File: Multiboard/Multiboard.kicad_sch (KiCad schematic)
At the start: 52 parts, among them J1 Conn_01x20_Socket, J2 Conn_01x20_Socket, J3 Debug, J4 USB_C_Receptacle_USB2.0_16P, SW1 BOOT0, SW2 NRST, SW8 KEY, U1 STM32F411RET6, U2 MAX662AESA_T, U3 MCP1792x-3302xCB, Y1 32.768KHz, Y2 25MHz

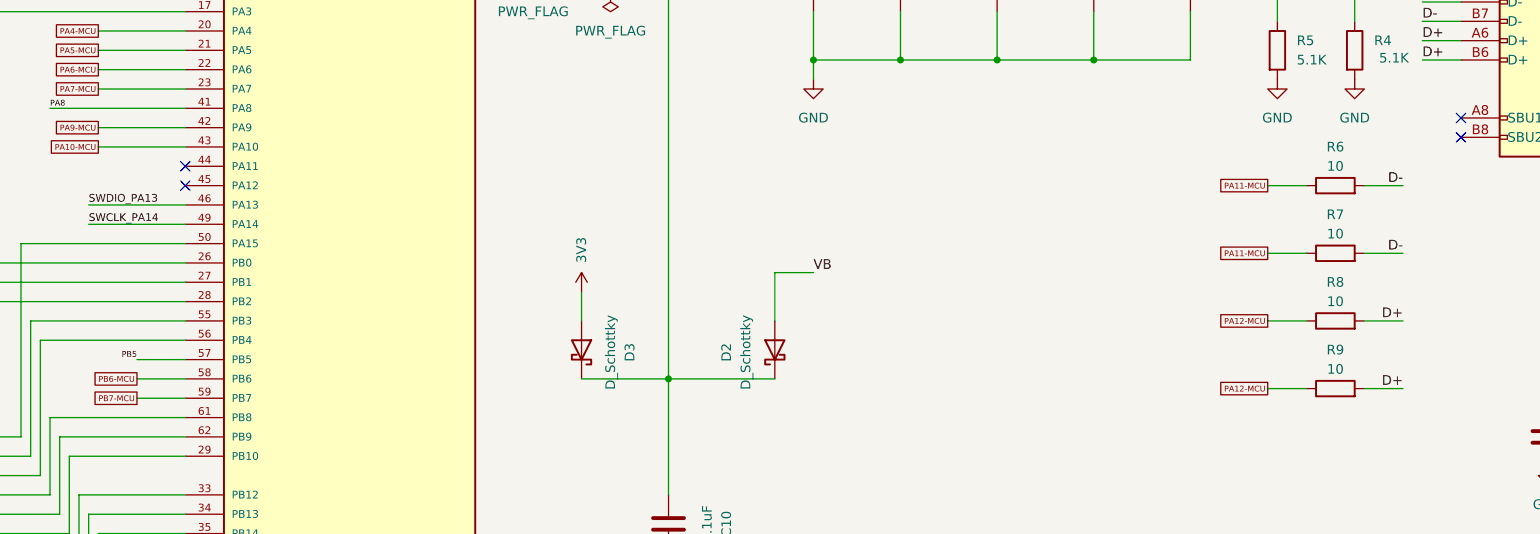
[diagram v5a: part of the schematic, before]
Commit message: positioned and wired ldo charge pump buttons leds and rtc circuit
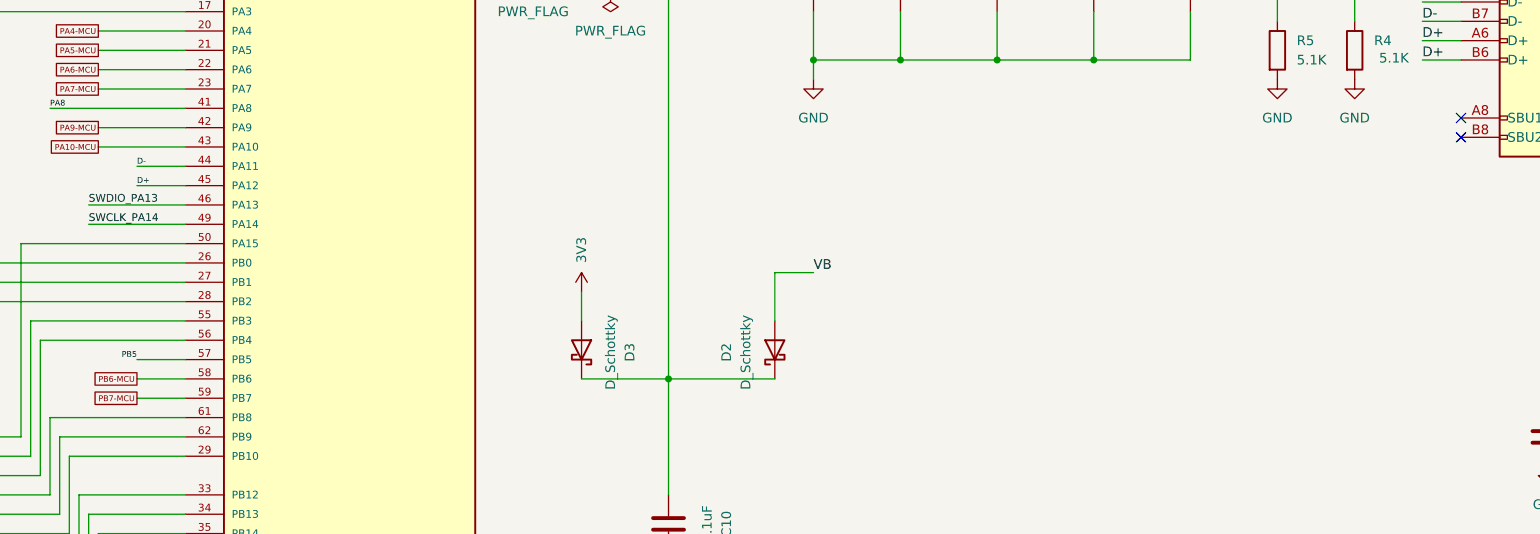
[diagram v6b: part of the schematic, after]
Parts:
- removed R6, R7, R8, R9: 10, Resistor_SMD:R_0603_1608Metric_Pad0.98x0.95mm_HandSolder, symbol Device:R
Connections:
- net D+: now also U1.45 (PA12)
- net D-: now also U1.44 (PA11)
- no-connect marks 14 -> 12

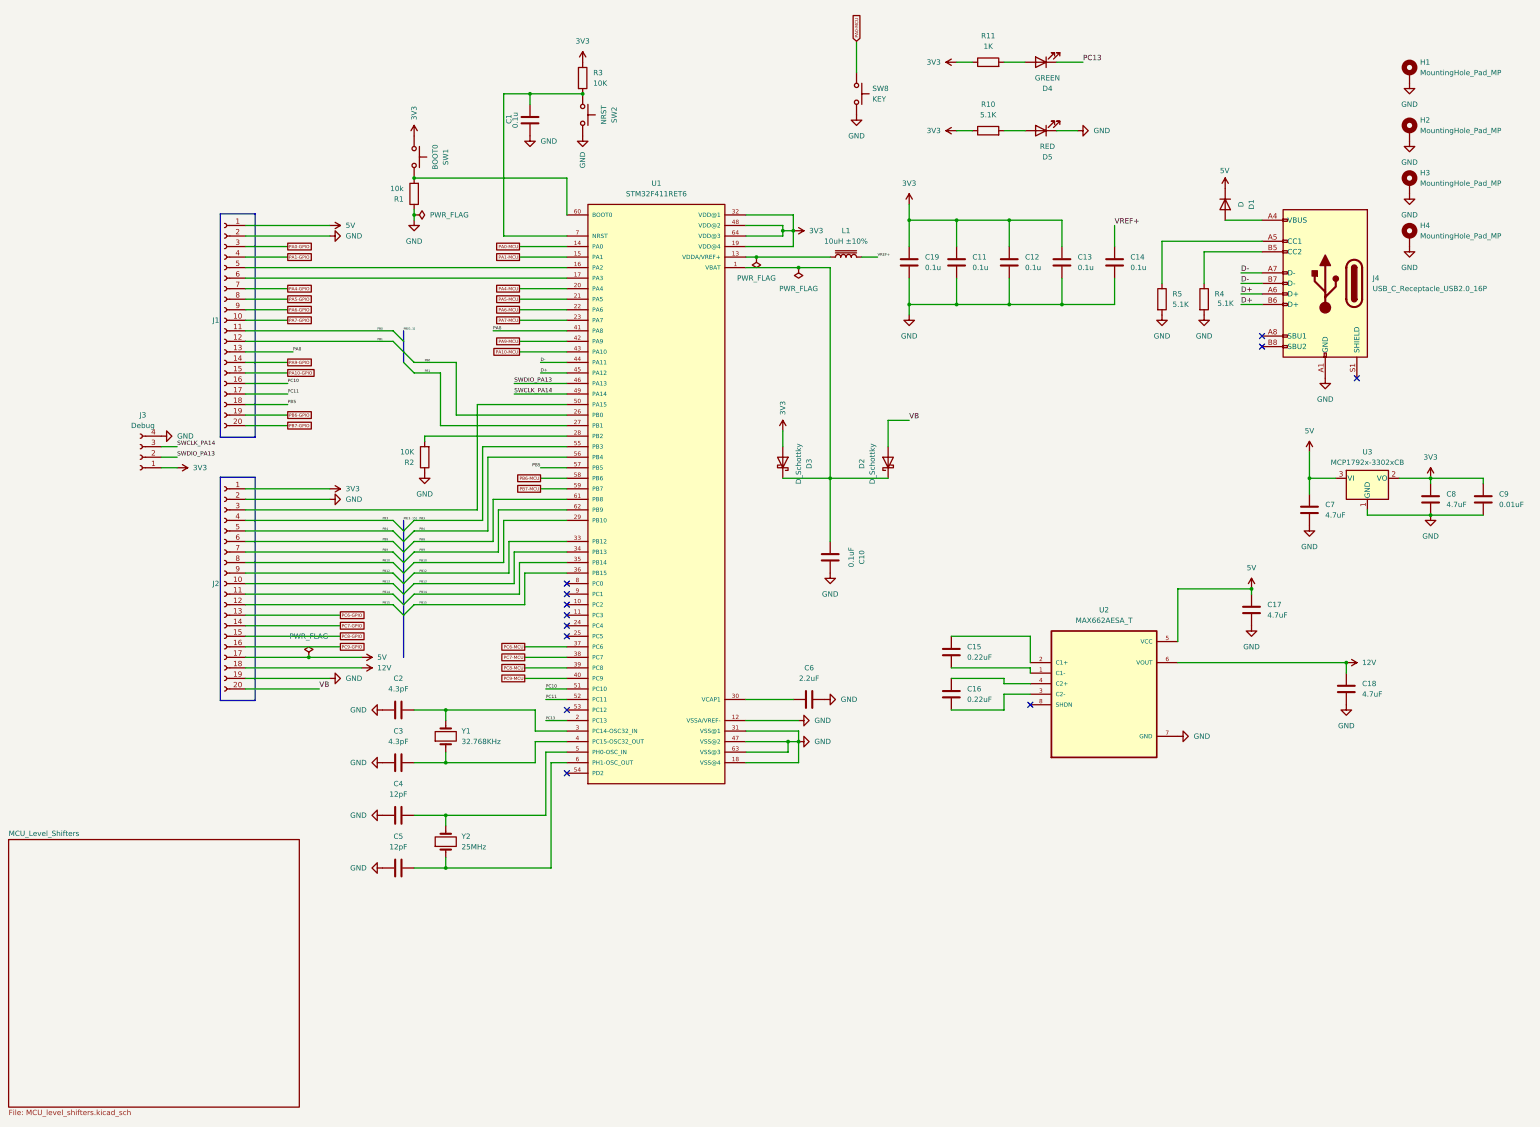
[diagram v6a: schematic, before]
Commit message: Wired usb
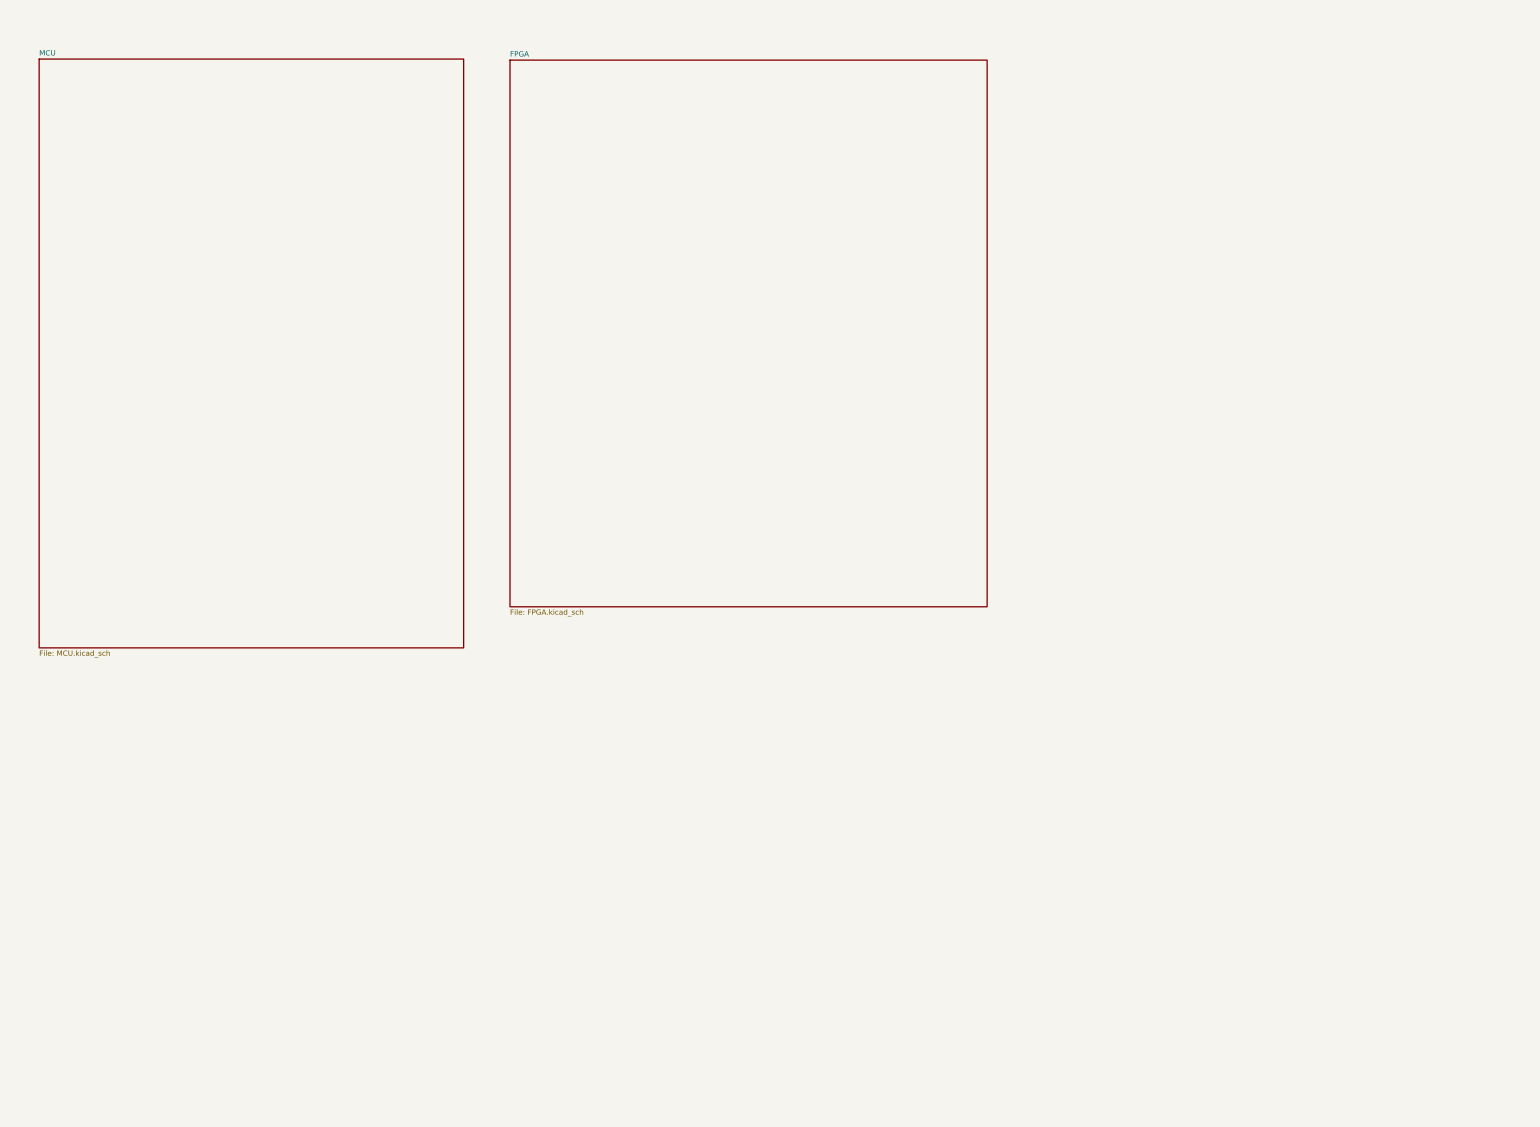
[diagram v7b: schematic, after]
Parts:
- removed C1, C11, C12, C13, C14, C19: 0.1u, Capacitor_SMD:C_0603_1608Metric_Pad1.08x0.95mm_HandSolder, symbol Device:C
- removed C10: 0.1uF, Capacitor_SMD:C_0603_1608Metric_Pad1.08x0.95mm_HandSolder, symbol Device:C
- removed C15, C16: 0.22uF, Capacitor_SMD:C_0603_1608Metric_Pad1.08x0.95mm_HandSolder, symbol Device:C
- removed C17, C18, C7, C8: 4.7uF, Capacitor_SMD:C_0603_1608Metric_Pad1.08x0.95mm_HandSolder, symbol Device:C
- removed C2, C3: 4.3pF, Capacitor_SMD:C_0603_1608Metric_Pad1.08x0.95mm_HandSolder, symbol Device:C
- removed C4, C5: 12pF, Capacitor_SMD:C_0603_1608Metric_Pad1.08x0.95mm_HandSolder, symbol Device:C
- removed C6: 2.2uF, Capacitor_SMD:C_0603_1608Metric_Pad1.08x0.95mm_HandSolder, symbol Device:C
- removed C9: 0.01uF, Capacitor_SMD:C_0603_1608Metric_Pad1.08x0.95mm_HandSolder, symbol Device:C
- removed D1: D, Diode_SMD:D_0603_1608Metric_Pad1.05x0.95mm_HandSolder, symbol Device:D
- removed D2, D3: D_Schottky, Diode_SMD:D_0603_1608Metric_Pad1.05x0.95mm_HandSolder, symbol Device:D_Schottky
- removed D4: GREEN, LED_SMD:LED_0603_1608Metric_Pad1.05x0.95mm_HandSolder, symbol Device:LED
- removed D5: RED, LED_SMD:LED_0603_1608Metric_Pad1.05x0.95mm_HandSolder, symbol Device:LED
- removed H1, H2, H3, H4: MountingHole_Pad_MP, MountingHole:MountingHole_3.2mm_M3_DIN965_Pad_TopBottom, symbol Mechanical:MountingHole_Pad_MP
- removed J1, J2: Conn_01x20_Socket, Connector_JST:JST_XA_B20B-XASK-1-A_1x20_P2.50mm_Vertical, symbol Connector:Conn_01x20_Socket
- removed J3: Debug, Connector_Hirose:Hirose_DF13-04P-1.25DSA_1x04_P1.25mm_Vertical, symbol Connector:Conn_01x04_Socket
- removed J4: USB_C_Receptacle_USB2.0_16P, Connector_USB:USB_C_Receptacle_G-Switch_GT-USB-7010ASV, symbol Connector:USB_C_Receptacle_USB2.0_16P
- removed L1: 10uH ±10%, Inductor_SMD:L_0603_1608Metric_Pad1.05x0.95mm_HandSolder, symbol Device:L_Iron
- removed R1: 10k, Resistor_SMD:R_0603_1608Metric_Pad0.98x0.95mm_HandSolder, symbol Device:R
- removed R10, R4, R5: 5.1K, Resistor_SMD:R_0603_1608Metric_Pad0.98x0.95mm_HandSolder, symbol Device:R
- removed R11: 1K, Resistor_SMD:R_0603_1608Metric_Pad0.98x0.95mm_HandSolder, symbol Device:R
- removed R2, R3: 10K, Resistor_SMD:R_0603_1608Metric_Pad0.98x0.95mm_HandSolder, symbol Device:R
- removed SW1: BOOT0, Button_Switch_THT:SW_PUSH_6mm, symbol Switch:SW_Push
- removed SW2: NRST, Button_Switch_THT:SW_PUSH_6mm, symbol Switch:SW_Push
- removed SW8: KEY, Button_Switch_THT:SW_PUSH_6mm, symbol Switch:SW_Push
- removed U1: STM32F411RET6, STM32F411RET6:QFP50P1200X1200X160-64N, symbol STM32F411RET6:STM32F411RET6
- removed U2: MAX662AESA_T, MAX662AESA+T:SOIC127P600X175-8N, symbol MAX662AESA_T:MAX662AESA_T
- removed U3: MCP1792x-3302xCB, Package_TO_SOT_SMD:SOT-23, symbol Regulator_Linear:MCP1792x-3302xCB
- removed Y1: 32.768KHz, Crystal:Crystal_SMD_3215-2Pin_3.2x1.5mm, symbol Device:Crystal
- removed Y2: 25MHz, Crystal:Crystal_SMD_HC49-SD, symbol Device:Crystal
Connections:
- no-connect marks 12 -> 0
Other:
- removed sheet MCU_Level_Shifters
- added sheet FPGA (FPGA.kicad_sch)
- added sheet MCU (MCU.kicad_sch)

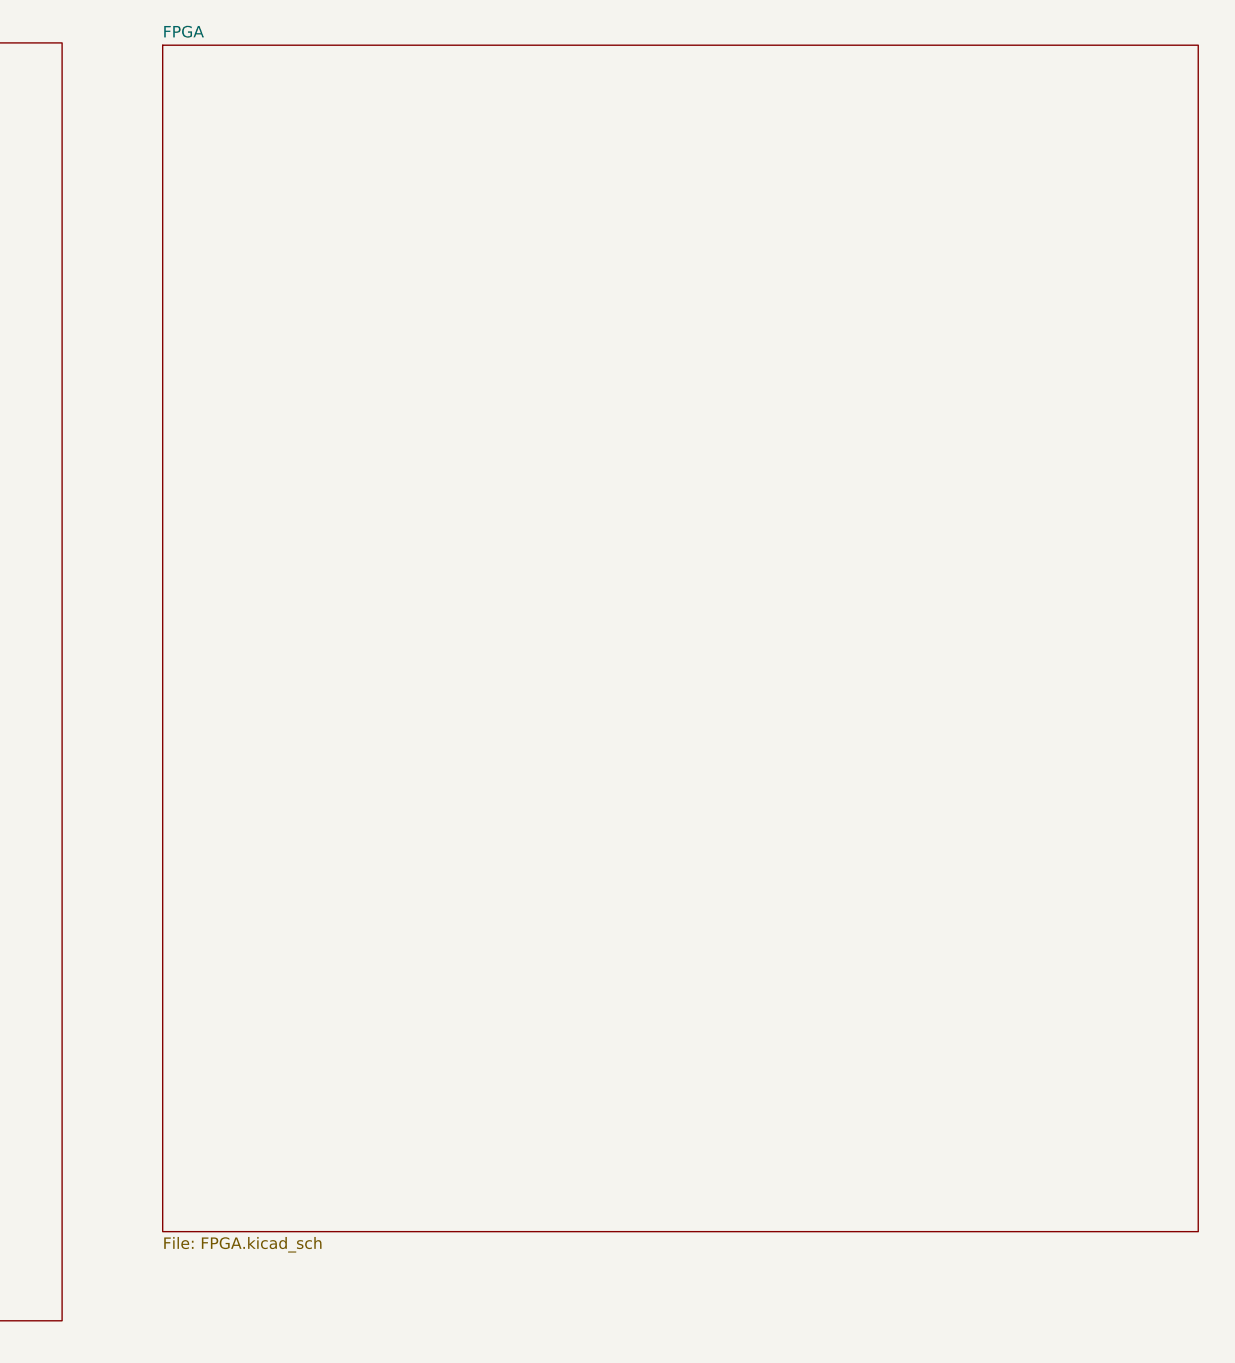
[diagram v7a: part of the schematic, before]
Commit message: Implemented FTDI in schematic
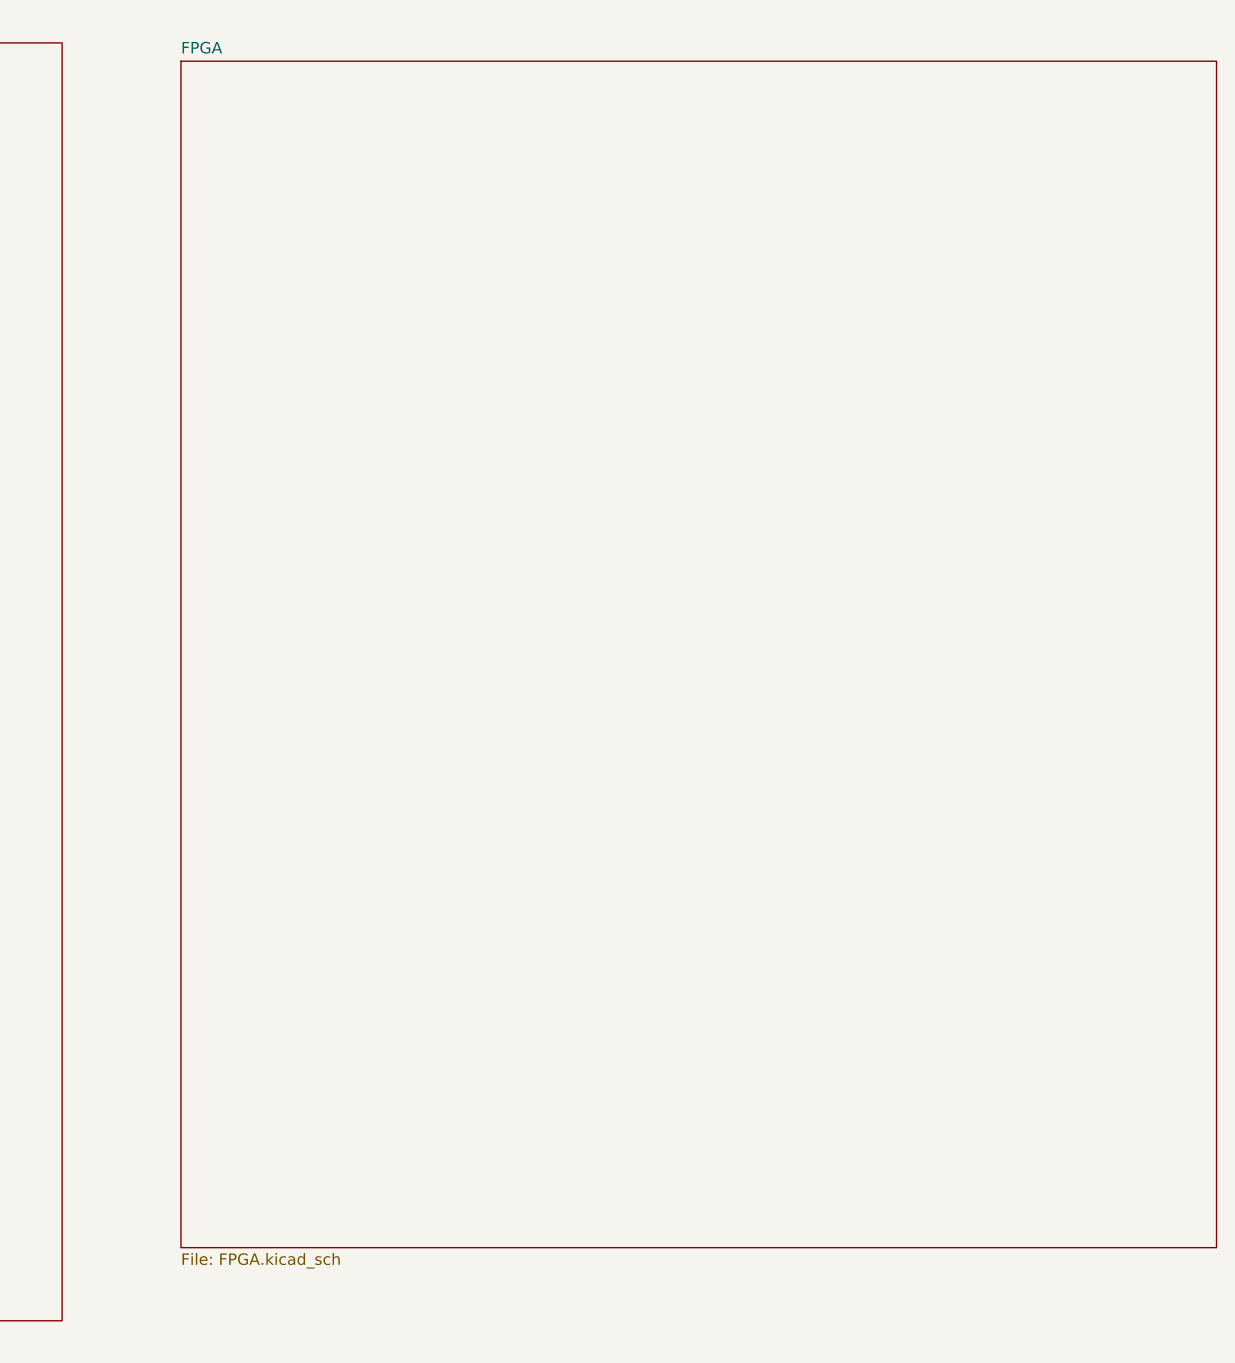
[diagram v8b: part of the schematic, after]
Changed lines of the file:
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@@
 	)
 	(sheet
-		(at 138.684 24.892)
+		(at 140.716 26.67)
 		(size 115.062 131.826)
 		(exclude_from_sim no)
@@
 		)
 		(property "Sheetname" "FPGA"
-			(at 138.684 24.1804 0)
+			(at 140.716 25.9584 0)
 			(effects
 				(font
@@
 		)
 		(property "Sheetfile" "FPGA.kicad_sch"
-			(at 138.684 157.3026 0)
+			(at 140.716 159.0806 0)
 			(effects
 				(font
